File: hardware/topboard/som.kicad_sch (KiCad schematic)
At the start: 8 parts

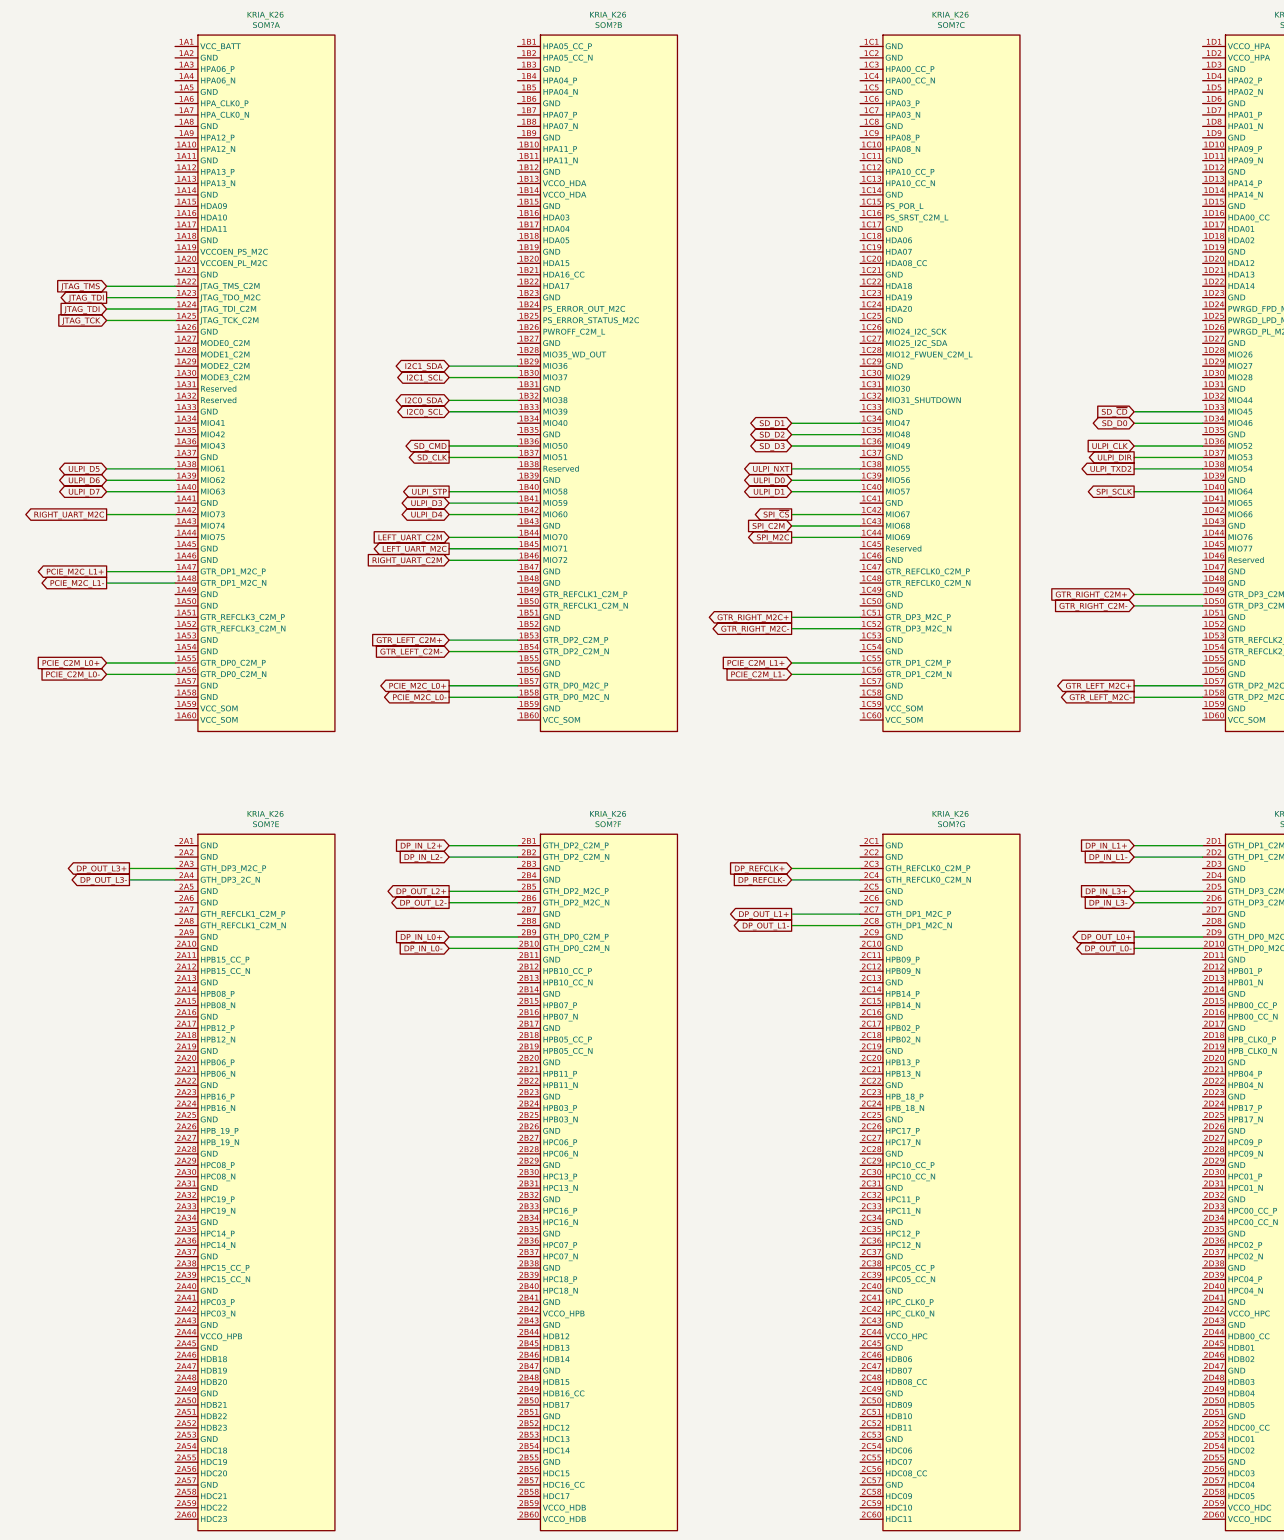
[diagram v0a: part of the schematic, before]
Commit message: Power and MIPI pin planning
Signed-off-by: gatecat <gatecat@ds0.me>
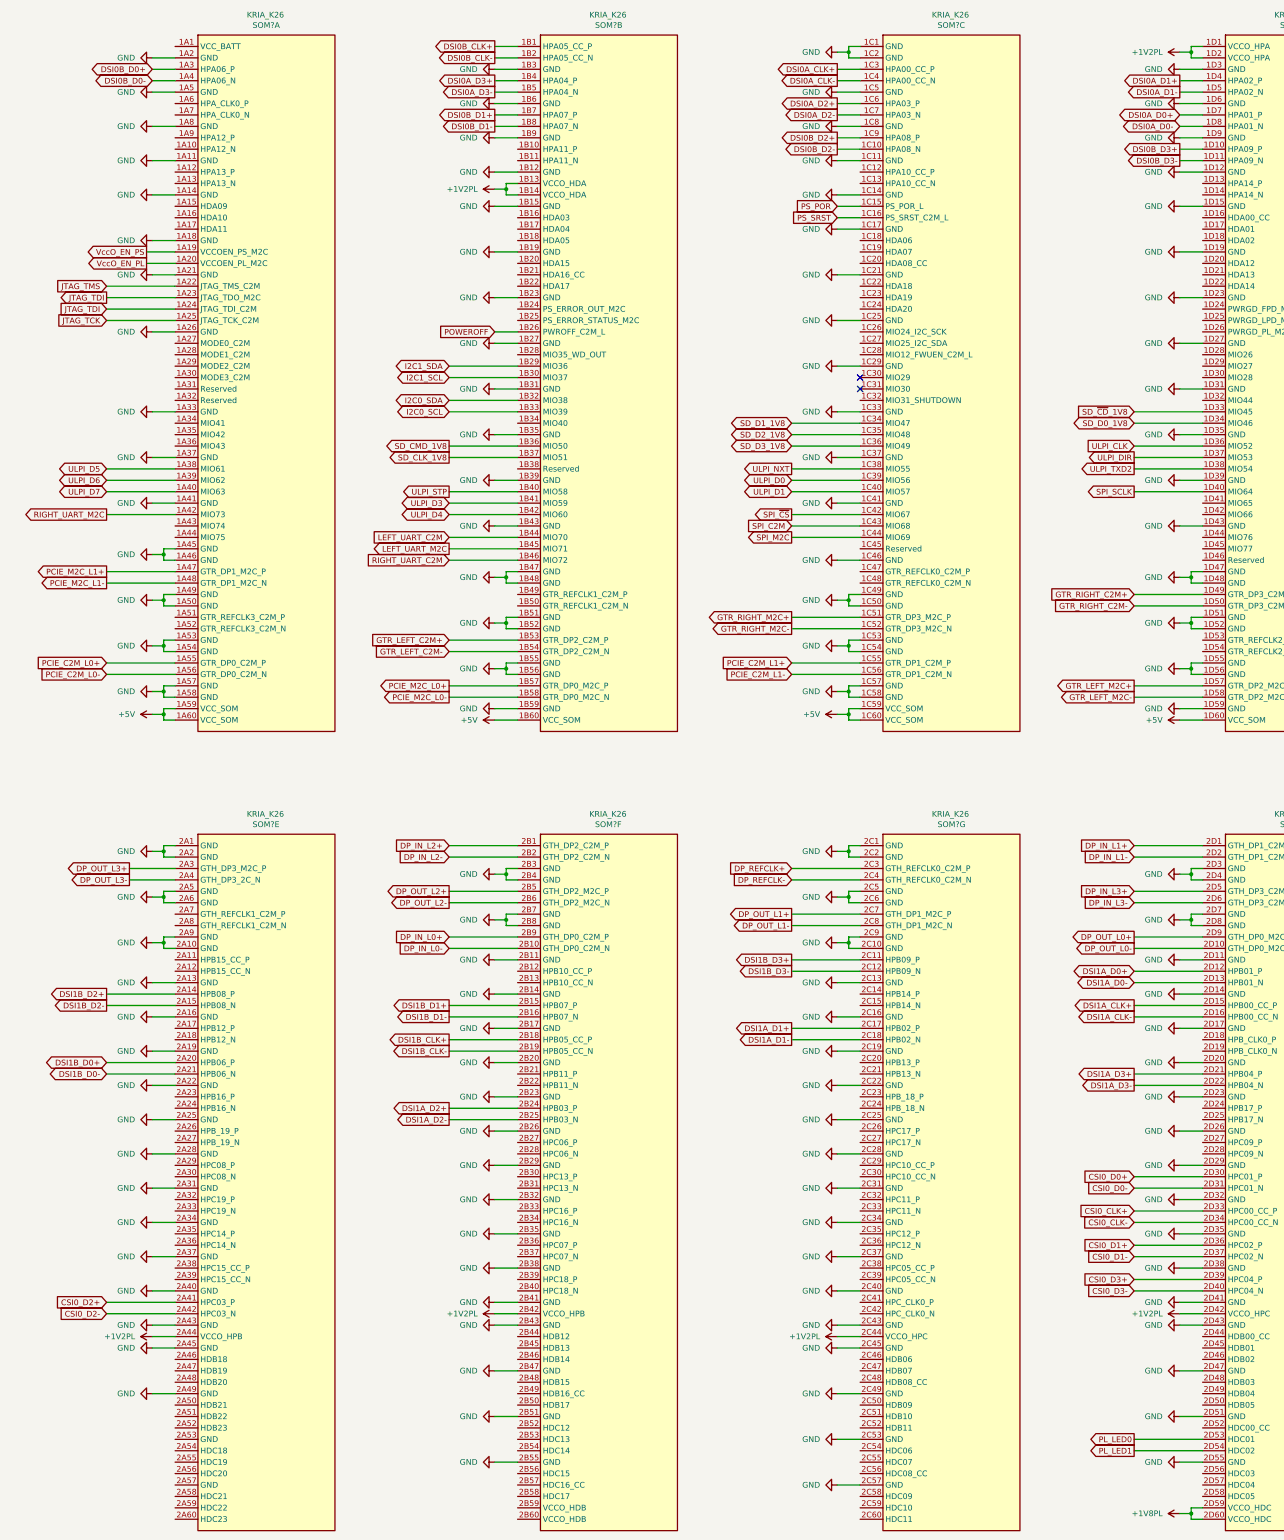
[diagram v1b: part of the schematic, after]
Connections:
- net GND: now reaches SOM?.2A1 (GND)
- net GND: now also SOM?.1A11 (GND), SOM?.1A14 (GND), SOM?.1A18 (GND), SOM?.1A2 (GND), SOM?.1A21 (GND), SOM?.1A26 (GND), SOM?.1A33 (GND), SOM?.1A37 (GND), SOM?.1A41 (GND), SOM?.1A45 (GND), SOM?.1A46 (GND), SOM?.1A49 (GND), SOM?.1A5 (GND), SOM?.1A50 (GND), SOM?.1A53 (GND), SOM?.1A54 (GND), SOM?.1A57 (GND), SOM?.1A58 (GND), SOM?.1A8 (GND), SOM?.1B12 (GND), SOM?.1B15 (GND), SOM?.1B19 (GND), SOM?.1B23 (GND), SOM?.1B27 (GND), SOM?.1B3 (GND), SOM?.1B31 (GND), SOM?.1B35 (GND), SOM?.1B39 (GND), SOM?.1B43 (GND), SOM?.1B47 (GND), SOM?.1B48 (GND), SOM?.1B51 (GND), SOM?.1B52 (GND), SOM?.1B55 (GND), SOM?.1B56 (GND), SOM?.1B59 (GND), SOM?.1B6 (GND), SOM?.1B9 (GND), SOM?.1C1 (GND), SOM?.1C11 (GND), SOM?.1C14 (GND), SOM?.1C17 (GND), SOM?.1C2 (GND), SOM?.1C21 (GND), SOM?.1C25 (GND), SOM?.1C29 (GND), SOM?.1C33 (GND), SOM?.1C37 (GND), SOM?.1C41 (GND), SOM?.1C46 (GND), SOM?.1C49 (GND), SOM?.1C5 (GND), SOM?.1C50 (GND), SOM?.1C53 (GND), SOM?.1C54 (GND), SOM?.1C57 (GND), SOM?.1C58 (GND), SOM?.1C8 (GND), SOM?.1D12 (GND), SOM?.1D15 (GND), SOM?.1D19 (GND), SOM?.1D23 (GND), SOM?.1D27 (GND), SOM?.1D3 (GND), SOM?.1D31 (GND), SOM?.1D35 (GND), SOM?.1D39 (GND), SOM?.1D43 (GND), SOM?.1D47 (GND), SOM?.1D48 (GND), SOM?.1D51 (GND), SOM?.1D52 (GND), SOM?.1D55 (GND), SOM?.1D56 (GND), SOM?.1D59 (GND), SOM?.1D6 (GND), SOM?.1D9 (GND), SOM?.2A10 (GND), SOM?.2A13 (GND), SOM?.2A16 (GND), SOM?.2A19 (GND), SOM?.2A2 (GND), SOM?.2A22 (GND), SOM?.2A25 (GND), SOM?.2A28 (GND), SOM?.2A31 (GND), SOM?.2A34 (GND), SOM?.2A37 (GND), SOM?.2A40 (GND), SOM?.2A43 (GND), SOM?.2A45 (GND), SOM?.2A49 (GND), SOM?.2A5 (GND), SOM?.2A6 (GND), SOM?.2A9 (GND), SOM?.2B11 (GND), SOM?.2B14 (GND), SOM?.2B17 (GND), SOM?.2B20 (GND), SOM?.2B23 (GND), SOM?.2B26 (GND), SOM?.2B29 (GND), SOM?.2B3 (GND), SOM?.2B32 (GND), SOM?.2B35 (GND), SOM?.2B38 (GND), SOM?.2B4 (GND), SOM?.2B41 (GND), SOM?.2B43 (GND), SOM?.2B47 (GND), SOM?.2B51 (GND), SOM?.2B55 (GND), SOM?.2B7 (GND), SOM?.2B8 (GND), SOM?.2C1 (GND), SOM?.2C10 (GND), SOM?.2C13 (GND), SOM?.2C16 (GND), SOM?.2C19 (GND), SOM?.2C2 (GND), SOM?.2C22 (GND), SOM?.2C25 (GND), SOM?.2C28 (GND), SOM?.2C31 (GND), SOM?.2C34 (GND), SOM?.2C37 (GND), SOM?.2C40 (GND), SOM?.2C43 (GND), SOM?.2C45 (GND), SOM?.2C49 (GND), SOM?.2C5 (GND), SOM?.2C53 (GND), SOM?.2C57 (GND), SOM?.2C6 (GND), SOM?.2C9 (GND), SOM?.2D11 (GND), SOM?.2D14 (GND), SOM?.2D17 (GND), SOM?.2D20 (GND), SOM?.2D23 (GND), SOM?.2D26 (GND), SOM?.2D29 (GND), SOM?.2D3 (GND), SOM?.2D32 (GND), SOM?.2D35 (GND), SOM?.2D38 (GND), SOM?.2D4 (GND), SOM?.2D41 (GND), SOM?.2D43 (GND), SOM?.2D47 (GND), SOM?.2D51 (GND), SOM?.2D55 (GND), SOM?.2D7 (GND), SOM?.2D8 (GND)
- net DSI1B_D2+: now reaches SOM?.2A14 (HPB08_P)
- net DSI1B_D2-: now reaches SOM?.2A15 (HPB08_N)
- net DSI1B_D0+: now reaches SOM?.2A20 (HPB06_P)
- net DSI1B_D0-: now reaches SOM?.2A21 (HPB06_N)
- net CSI0_D2+: now reaches SOM?.2A41 (HPC03_P)
- net CSI0_D2-: now reaches SOM?.2A42 (HPC03_N)
- net +1V2PL: now reaches SOM?.2A44 (VCCO_HPB)
- net +1V2PL: now also SOM?.1B13 (VCCO_HDA), SOM?.1B14 (VCCO_HDA), SOM?.1D1 (VCCO_HPA), SOM?.1D2 (VCCO_HPA), SOM?.2B42 (VCCO_HPB), SOM?.2C44 (VCCO_HPC), SOM?.2D42 (VCCO_HPC)
- net DSI0B_D2-: now reaches SOM?.1C10 (HPA08_N)
- net PS_POR: now reaches SOM?.1C15 (PS_POR_L)
- net PS_SRST: now reaches SOM?.1C16 (PS_SRST_C2M_L)
- net DSI0A_CLK+: now reaches SOM?.1C3 (HPA00_CC_P)
- net DSI0A_CLK-: now reaches SOM?.1C4 (HPA00_CC_N)
- net +5V: now reaches SOM?.1C59 (VCC_SOM)
- net +5V: now also SOM?.1A59 (VCC_SOM), SOM?.1A60 (VCC_SOM), SOM?.1B60 (VCC_SOM), SOM?.1C60 (VCC_SOM), SOM?.1D60 (VCC_SOM)
- net DSI0A_D2+: now reaches SOM?.1C6 (HPA03_P)
- net DSI0A_D2-: now reaches SOM?.1C7 (HPA03_N)
- net DSI0B_D2+: now reaches SOM?.1C9 (HPA08_P)
- net DSI0B_D3+: now reaches SOM?.1D10 (HPA09_P)
- net DSI0B_D3-: now reaches SOM?.1D11 (HPA09_N)
- net DSI0A_D1+: now reaches SOM?.1D4 (HPA02_P)
- net DSI0A_D1-: now reaches SOM?.1D5 (HPA02_N)
- net DSI0A_D0+: now reaches SOM?.1D7 (HPA01_P)
- net DSI0A_D0-: now reaches SOM?.1D8 (HPA01_N)
- net VccO_EN_PS: now reaches SOM?.1A19 (VCCOEN_PS_M2C)
- net VccO_EN_PL: now reaches SOM?.1A20 (VCCOEN_PL_M2C)
- net DSI0B_D0+: now reaches SOM?.1A3 (HPA06_P)
- net DSI0B_D0-: now reaches SOM?.1A4 (HPA06_N)
- net DSI0B_CLK+: now reaches SOM?.1B1 (HPA05_CC_P)
- net DSI0B_CLK-: now reaches SOM?.1B2 (HPA05_CC_N)
- net POWEROFF: now reaches SOM?.1B26 (PWROFF_C2M_L)
- net DSI0A_D3+: now reaches SOM?.1B4 (HPA04_P)
- net DSI0A_D3-: now reaches SOM?.1B5 (HPA04_N)
- net DSI0B_D1+: now reaches SOM?.1B7 (HPA07_P)
- net DSI0B_D1-: now reaches SOM?.1B8 (HPA07_N)
- net DSI1A_D0+: now reaches SOM?.2D12 (HPB01_P)
- net DSI1A_D0-: now reaches SOM?.2D13 (HPB01_N)
- net DSI1A_CLK+: now reaches SOM?.2D15 (HPB00_CC_P)
- net DSI1A_CLK-: now reaches SOM?.2D16 (HPB00_CC_N)
- net DSI1A_D3+: now reaches SOM?.2D21 (HPB04_P)
- net DSI1A_D3-: now reaches SOM?.2D22 (HPB04_N)
- net CSI0_D0+: now reaches SOM?.2D30 (HPC01_P)
- net CSI0_D0-: now reaches SOM?.2D31 (HPC01_N)
- net CSI0_CLK+: now reaches SOM?.2D33 (HPC00_CC_P)
- net CSI0_CLK-: now reaches SOM?.2D34 (HPC00_CC_N)
- net CSI0_D1+: now reaches SOM?.2D36 (HPC02_P)
- net CSI0_D1-: now reaches SOM?.2D37 (HPC02_N)
- net CSI0_D3+: now reaches SOM?.2D39 (HPC04_P)
- net CSI0_D3-: now reaches SOM?.2D40 (HPC04_N)
- net PL_LED0: now reaches SOM?.2D53 (HDC01)
- net PL_LED1: now reaches SOM?.2D54 (HDC02)
- net +1V8PL: now reaches SOM?.2D59 (VCCO_HDC)
- net +1V8PL: now also SOM?.2D60 (VCCO_HDC)
- net DSI1B_D3+: now reaches SOM?.2C11 (HPB09_P)
- net DSI1B_D3-: now reaches SOM?.2C12 (HPB09_N)
- net DSI1A_D1+: now reaches SOM?.2C17 (HPB02_P)
- net DSI1A_D1-: now reaches SOM?.2C18 (HPB02_N)
- net DSI1B_D1+: now reaches SOM?.2B15 (HPB07_P)
- net DSI1B_D1-: now reaches SOM?.2B16 (HPB07_N)
- net DSI1B_CLK+: now reaches SOM?.2B18 (HPB05_CC_P)
- net DSI1B_CLK-: now reaches SOM?.2B19 (HPB05_CC_N)
- net DSI1A_D2+: now reaches SOM?.2B24 (HPB03_P)
- net DSI1A_D2-: now reaches SOM?.2B25 (HPB03_N)
- net SD_CLK renamed SD_CLK_1V8
- net SD_CMD renamed SD_CMD_1V8
- net SD_D0 renamed SD_D0_1V8
- net SD_D1 renamed SD_D1_1V8
- net SD_D2 renamed SD_D2_1V8
- net SD_D3 renamed SD_D3_1V8
- net SD_~{CD} renamed SD_~{CD}_1V8
- no-connect marks 0 -> 2

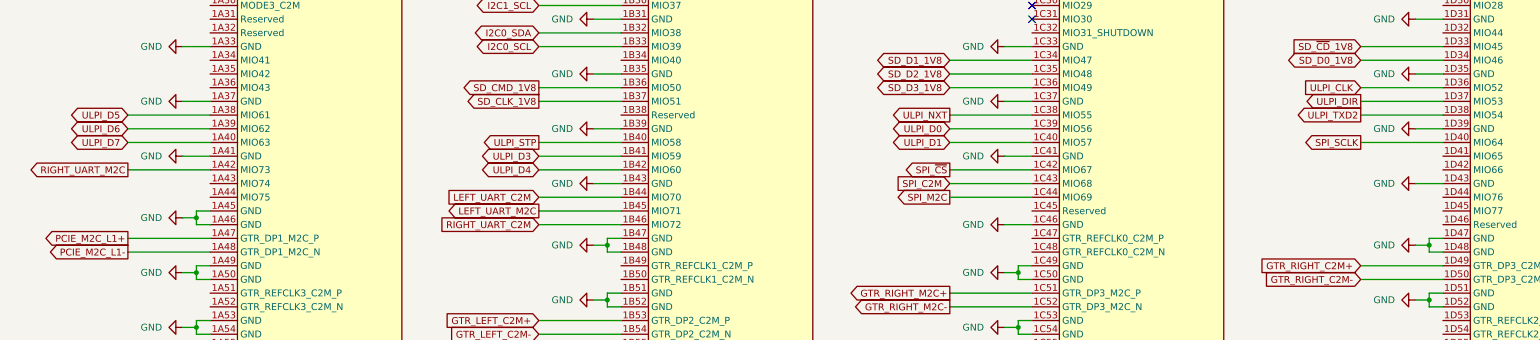
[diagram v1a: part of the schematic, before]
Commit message: SD card, ULPI PHY, JTAG/UART
Signed-off-by: gatecat <gatecat@ds0.me>
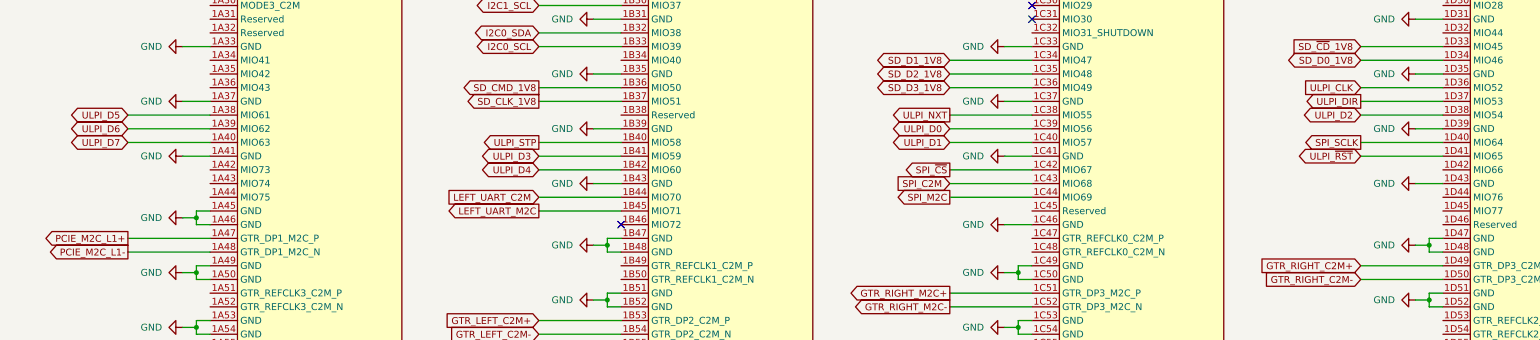
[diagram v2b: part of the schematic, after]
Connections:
- net ULPI_~{RST}: now reaches SOM?.1D41 (MIO65)
- net RIGHT_UART_C2M: no longer names the net of SOM?.1B46 (MIO72)
- net RIGHT_UART_M2C: no longer names the net of SOM?.1A42 (MIO73)
- net ULPI_TXD2 renamed ULPI_D2
- no-connect marks 2 -> 3
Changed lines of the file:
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@@
   (junction (at 342.9 222.25) (diameter 0) (color 0 0 0 0))
   (junction (at 342.9 354.33) (diameter 0) (color 0 0 0 0))
+  (no_connect (at 193.04 142.24))
   (no_connect (at 269.24 101.6))
   (no_connect (at 269.24 104.14))
@@
     (stroke (width 0) (type default) (color 0 0 0 0))
   )
-  (wire (pts (xy 101.6 132.08) (xy 116.84 132.08))
-    (stroke (width 0) (type default) (color 0 0 0 0))
-  )
   (wire (pts (xy 101.6 144.78) (xy 116.84 144.78))
     (stroke (width 0) (type default) (color 0 0 0 0))
@@
     (stroke (width 0) (type default) (color 0 0 0 0))
   )
-  (wire (pts (xy 177.8 142.24) (xy 193.04 142.24))
-    (stroke (width 0) (type default) (color 0 0 0 0))
-  )
   (wire (pts (xy 177.8 160.02) (xy 193.04 160.02))
     (stroke (width 0) (type default) (color 0 0 0 0))
@@
     (stroke (width 0) (type default) (color 0 0 0 0))
   )
+  (wire (pts (xy 330.2 129.54) (xy 345.44 129.54))
+    (stroke (width 0) (type default) (color 0 0 0 0))
+  )
   (wire (pts (xy 330.2 149.86) (xy 345.44 149.86))
     (stroke (width 0) (type default) (color 0 0 0 0))
@@
     )
   )
-  (global_label "RIGHT_UART_M2C" (shape output) (at 101.6 132.08 180) (fields_autoplaced)
-    (effects (font (size 1.27 1.27)) (justify right))
-    (property "Intersheet References" "${INTERSHEET_REFS}" (id 0) (at 83.2212 132.0006 0)
-      (effects (font (size 1.27 1.27)) (justify right) hide)
-    )
-  )
   (global_label "PCIE_M2C_L1+" (shape output) (at 101.6 144.78 180) (fields_autoplaced)
     (effects (font (size 1.27 1.27)) (justify right))
@@
     )
   )
-  (global_label "RIGHT_UART_C2M" (shape input) (at 177.8 142.24 180) (fields_autoplaced)
-    (effects (font (size 1.27 1.27)) (justify right))
-    (property "Intersheet References" "${INTERSHEET_REFS}" (id 0) (at 159.4212 142.1606 0)
-      (effects (font (size 1.27 1.27)) (justify right) hide)
-    )
-  )
   (global_label "GTR_LEFT_C2M+" (shape input) (at 177.8 160.02 180) (fields_autoplaced)
     (effects (font (size 1.27 1.27)) (justify right))
@@
     )
   )
-  (global_label "ULPI_TXD2" (shape output) (at 330.2 121.92 180) (fields_autoplaced)
-    (effects (font (size 1.27 1.27)) (justify right))
-    (property "Intersheet References" "${INTERSHEET_REFS}" (id 0) (at 317.9293 121.8406 0)
+  (global_label "ULPI_D2" (shape bidirectional) (at 330.2 121.92 180) (fields_autoplaced)
+    (effects (font (size 1.27 1.27)) (justify right))
+    (property "Intersheet References" "${INTERSHEET_REFS}" (id 0) (at 320.1064 121.8406 0)
       (effects (font (size 1.27 1.27)) (justify right) hide)
     )
@@
       (effects (font (size 1.27 1.27)) (justify right) hide)
     )
+  )
+  (global_label "ULPI_~{RST}" (shape bidirectional) (at 330.2 129.54 180) (fields_autoplaced)
+    (effects (font (size 1.27 1.27)) (justify right))
+    (property "Intersheet References" "${INTERSHEET_REFS}" (id 0) (at 319.1388 129.4606 0)
+      (effects (font (size 1.27 1.27)) (justify right) hide)
+    )
